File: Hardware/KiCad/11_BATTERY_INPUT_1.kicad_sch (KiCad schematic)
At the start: 0 parts

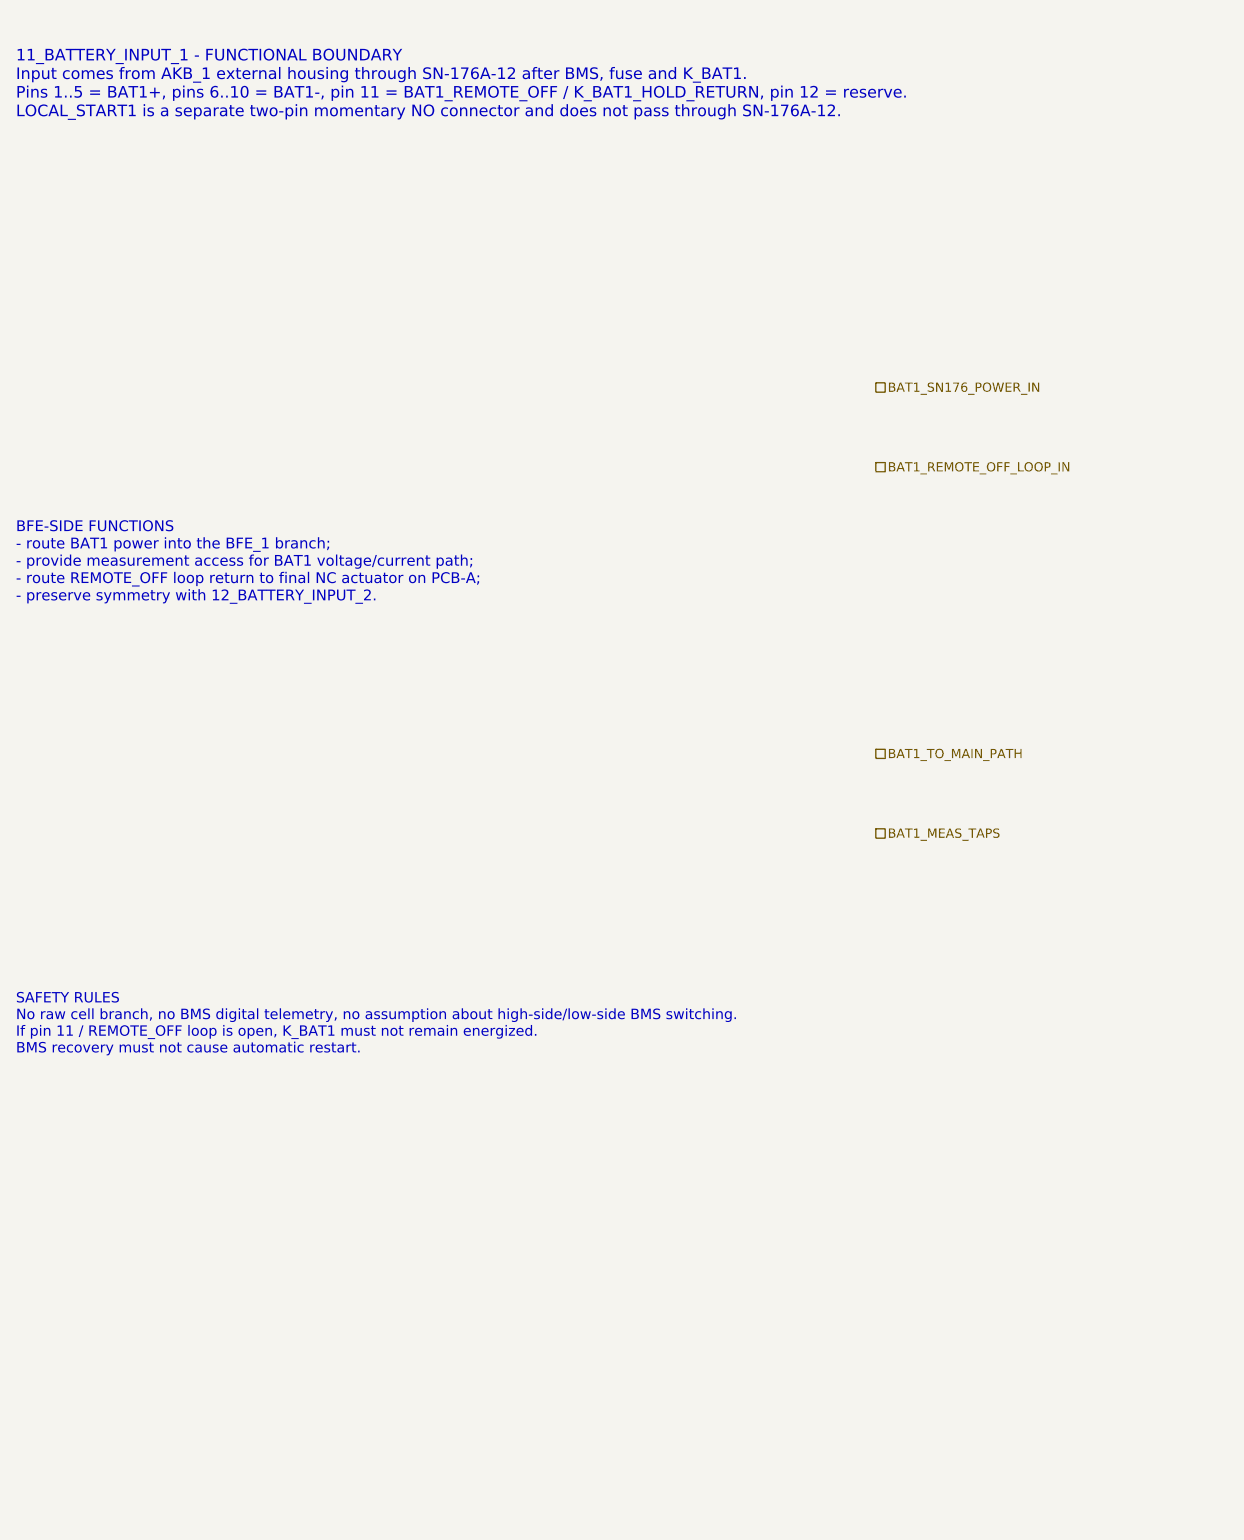
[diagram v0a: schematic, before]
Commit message: hardware: refine BAT1 input boundary level B
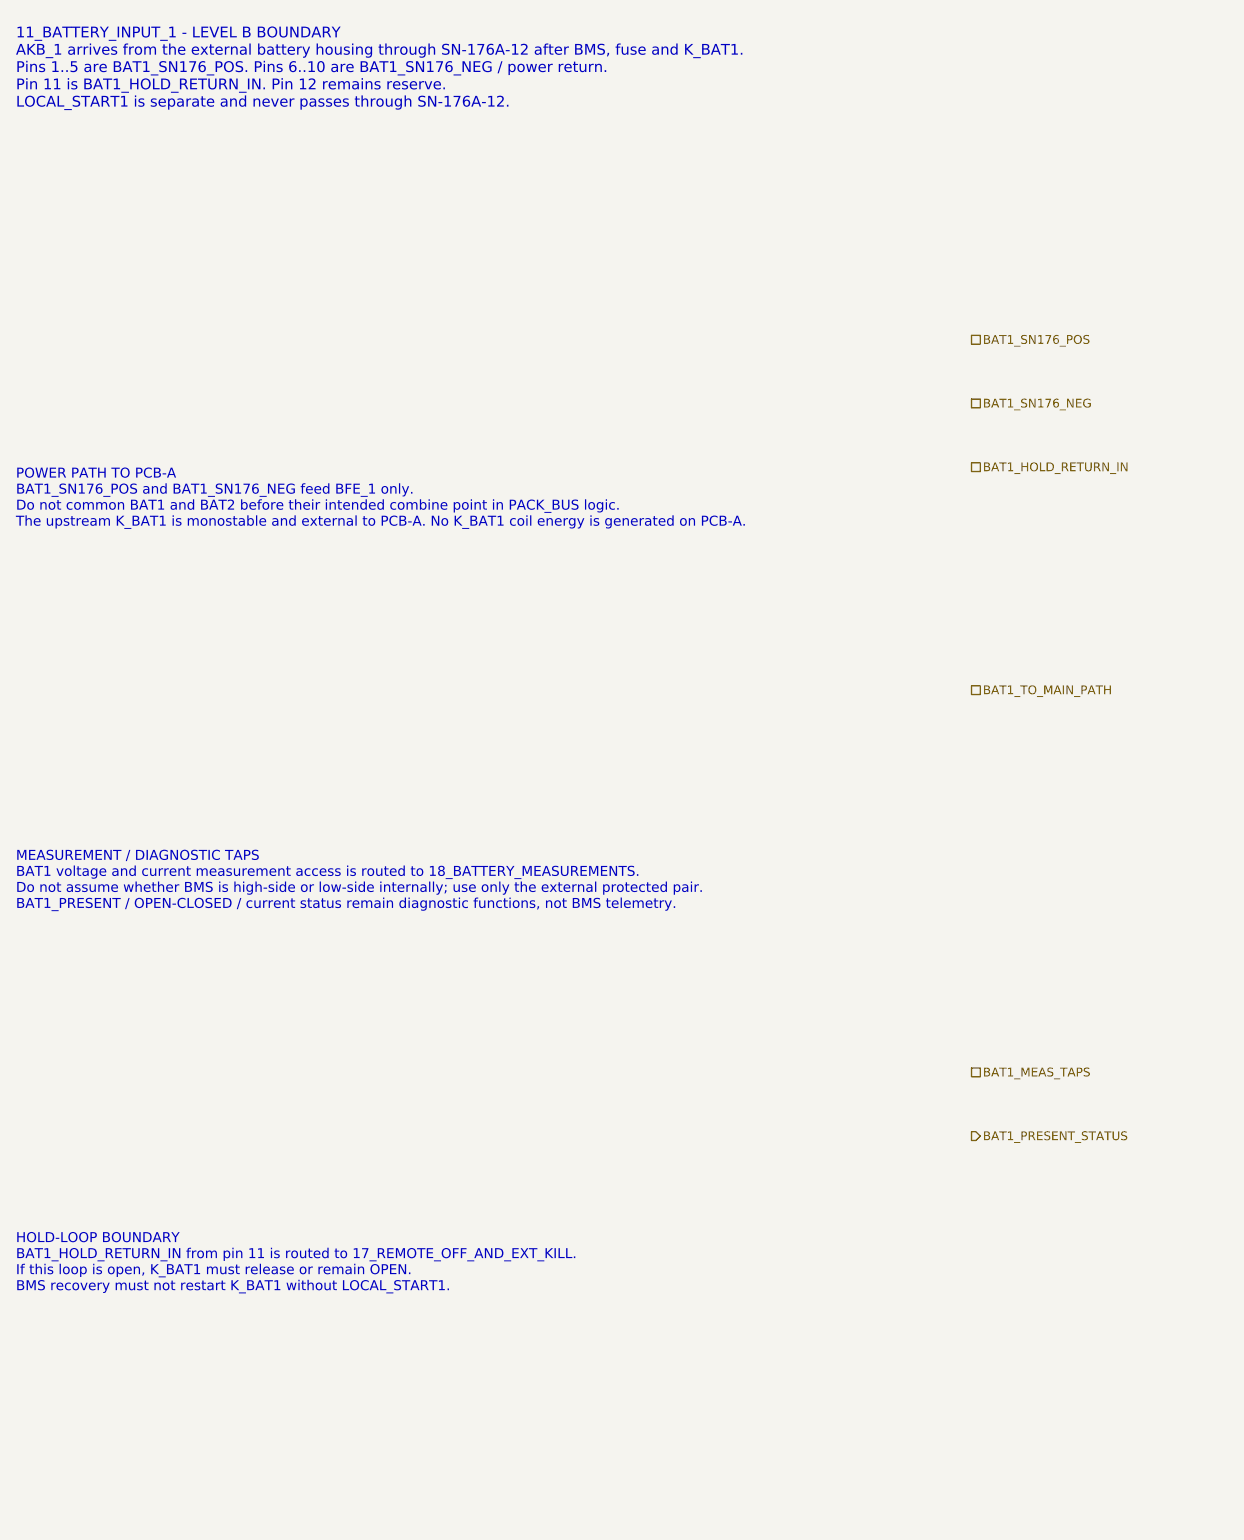
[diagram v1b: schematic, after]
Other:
- note added: "11_BATTERY_INPUT_1 - LEVEL B BOUNDARY AKB_1 arrives from the external battery housing through SN-176A-12 after BMS, fuse and K_BAT1. Pins 1..5 are BAT1_SN176_POS. Pins 6..10 are BAT1_SN176_NEG / power return. Pin 11 is BAT1_HOLD_RETURN_IN. Pin 12 remains reserve. LOCAL_START1 is separate and never passes through SN-176A-12."
- note added: "HOLD-LOOP BOUNDARY BAT1_HOLD_RETURN_IN from pin 11 is routed to 17_REMOTE_OFF_AND_EXT_KILL. If this loop is open, K_BAT1 must release or remain OPEN. BMS recovery must not restart K_BAT1 without LOCAL_START1."
- note added: "MEASUREMENT / DIAGNOSTIC TAPS BAT1 voltage and current measurement access is routed to 18_BATTERY_MEASUREMENTS. Do not assume whether BMS is high-side or low-side internally; use only the external protected pair. BAT1_PRESENT / OPEN-CLOSED / current status remain diagnostic functions, not BMS telemetry."
- note added: "POWER PATH TO PCB-A BAT1_SN176_POS and BAT1_SN176_NEG feed BFE_1 only. Do not common BAT1 and BAT2 before their intended combine point in PACK_BUS logic. The upstream K_BAT1 is monostable and external to PCB-A. No K_BAT1 coil energy is generated on PCB-A."
- note removed: "11_BATTERY_INPUT_1 - FUNCTIONAL BOUNDARY Input comes from AKB_1 external housing through SN-176A-12 after BMS, fuse and K_BAT1. Pins 1..5 = BAT1+, pins 6..10 = BAT1-, pin 11 = BAT1_REMOTE_OFF / K_BAT1_HOLD_RETURN, pin 12 = reserve. LOCAL_START1 is a separate two-pin momentary NO connector and does not pass through SN-176A-12."
- note removed: "BFE-SIDE FUNCTIONS - route BAT1 power into the BFE_1 branch; - provide measurement access for BAT1 voltage/current path; - route REMOTE_OFF loop return to final NC actuator on PCB-A; - preserve symmetry with 12_BATTERY_INPUT_2."
- note removed: "SAFETY RULES No raw cell branch, no BMS digital telemetry, no assumption about high-side/low-side BMS switching. If pin 11 / REMOTE_OFF loop is open, K_BAT1 must not remain energized. BMS recovery must not cause automatic restart."
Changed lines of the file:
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@@
 		(title "11_BATTERY_INPUT_1 - BFE input from AKB_1")
 		(date "2026-07-15")
-		(rev "A1")
+		(rev "B1")
 		(company "Gonoboben/plataVM")
-		(comment 1 "Architecture Level A: BFE-side input boundary for battery 1")
+		(comment 1 "Architecture Level B: BAT1 connector boundary and net naming")
 		(comment 2 "No connector family, fuse, current sensor or contactor model selected here")
 	)
-	(text "11_BATTERY_INPUT_1 - FUNCTIONAL BOUNDARY\nInput comes from AKB_1 external housing through SN-176A-12 after BMS, fuse and K_BAT1.\nPins 1..5 = BAT1+, pins 6..10 = BAT1-, pin 11 = BAT1_REMOTE_OFF / K_BAT1_HOLD_RETURN, pin 12 = reserve.\nLOCAL_START1 is a separate two-pin momentary NO connector and does not pass through SN-176A-12."
+	(text "11_BATTERY_INPUT_1 - LEVEL B BOUNDARY\nAKB_1 arrives from the external battery housing through SN-176A-12 after BMS, fuse and K_BAT1.\nPins 1..5 are BAT1_SN176_POS. Pins 6..10 are BAT1_SN176_NEG / power return.\nPin 11 is BAT1_HOLD_RETURN_IN. Pin 12 remains reserve.\nLOCAL_START1 is separate and never passes through SN-176A-12."
 		(exclude_from_sim no)
-		(at 12 18 0)
-		(effects (font (size 1.45 1.45)) (justify left))
+		(at 12 16 0)
+		(effects (font (size 1.35 1.35)) (justify left))
 		(uuid "bfe-dh-00000011-0000-4000-8000-000000000101")
 	)
-	(text "BFE-SIDE FUNCTIONS\n- route BAT1 power into the BFE_1 branch;\n- provide measurement access for BAT1 voltage/current path;\n- route REMOTE_OFF loop return to final NC actuator on PCB-A;\n- preserve symmetry with 12_BATTERY_INPUT_2."
+	(text "POWER PATH TO PCB-A\nBAT1_SN176_POS and BAT1_SN176_NEG feed BFE_1 only.\nDo not common BAT1 and BAT2 before their intended combine point in PACK_BUS logic.\nThe upstream K_BAT1 is monostable and external to PCB-A. No K_BAT1 coil energy is generated on PCB-A."
 		(exclude_from_sim no)
-		(at 12 78 0)
-		(effects (font (size 1.35 1.35)) (justify left))
+		(at 12 70 0)
+		(effects (font (size 1.25 1.25)) (justify left))
 		(uuid "bfe-dh-00000011-0000-4000-8000-000000000102")
 	)
-	(text "SAFETY RULES\nNo raw cell branch, no BMS digital telemetry, no assumption about high-side/low-side BMS switching.\nIf pin 11 / REMOTE_OFF loop is open, K_BAT1 must not remain energized.\nBMS recovery must not cause automatic restart."
+	(text "MEASUREMENT / DIAGNOSTIC TAPS\nBAT1 voltage and current measurement access is routed to 18_BATTERY_MEASUREMENTS.\nDo not assume whether BMS is high-side or low-side internally; use only the external protected pair.\nBAT1_PRESENT / OPEN-CLOSED / current status remain diagnostic functions, not BMS telemetry."
 		(exclude_from_sim no)
-		(at 12 136 0)
-		(effects (font (size 1.3 1.3)) (justify left))
+		(at 12 118 0)
+		(effects (font (size 1.25 1.25)) (justify left))
 		(uuid "bfe-dh-00000011-0000-4000-8000-000000000103")
 	)
-	(hierarchical_label "BAT1_SN176_POWER_IN" (shape passive) (exclude_from_sim no) (at 120 56 0) (effects (font (size 1.15 1.15)) (justify left)) (uuid "bfe-dh-00000011-0000-4000-8000-000000000201"))
-	(hierarchical_label "BAT1_REMOTE_OFF_LOOP_IN" (shape passive) (exclude_from_sim no) (at 120 66 0) (effects (font (size 1.15 1.15)) (justify left)) (uuid "bfe-dh-00000011-0000-4000-8000-000000000202"))
-	(hierarchical_label "BAT1_TO_MAIN_PATH" (shape passive) (exclude_from_sim no) (at 120 102 0) (effects (font (size 1.15 1.15)) (justify left)) (uuid "bfe-dh-00000011-0000-4000-8000-000000000203"))
-	(hierarchical_label "BAT1_MEAS_TAPS" (shape passive) (exclude_from_sim no) (at 120 112 0) (effects (font (size 1.15 1.15)) (justify left)) (uuid "bfe-dh-00000011-0000-4000-8000-000000000204"))
+	(text "HOLD-LOOP BOUNDARY\nBAT1_HOLD_RETURN_IN from pin 11 is routed to 17_REMOTE_OFF_AND_EXT_KILL.\nIf this loop is open, K_BAT1 must release or remain OPEN.\nBMS recovery must not restart K_BAT1 without LOCAL_START1."
+		(exclude_from_sim no)
+		(at 12 166 0)
+		(effects (font (size 1.25 1.25)) (justify left))
+		(uuid "bfe-dh-00000011-0000-4000-8000-000000000104")
+	)
+	(hierarchical_label "BAT1_SN176_POS" (shape passive) (exclude_from_sim no) (at 132 50 0) (effects (font (size 1.1 1.1)) (justify left)) (uuid "bfe-dh-00000011-0000-4000-8000-000000000201"))
+	(hierarchical_label "BAT1_SN176_NEG" (shape passive) (exclude_from_sim no) (at 132 58 0) (effects (font (size 1.1 1.1)) (justify left)) (uuid "bfe-dh-00000011-0000-4000-8000-000000000202"))
+	(hierarchical_label "BAT1_HOLD_RETURN_IN" (shape passive) (exclude_from_sim no) (at 132 66 0) (effects (font (size 1.1 1.1)) (justify left)) (uuid "bfe-dh-00000011-0000-4000-8000-000000000203"))
+	(hierarchical_label "BAT1_TO_MAIN_PATH" (shape passive) (exclude_from_sim no) (at 132 94 0) (effects (font (size 1.1 1.1)) (justify left)) (uuid "bfe-dh-00000011-0000-4000-8000-000000000204"))
+	(hierarchical_label "BAT1_MEAS_TAPS" (shape passive) (exclude_from_sim no) (at 132 142 0) (effects (font (size 1.1 1.1)) (justify left)) (uuid "bfe-dh-00000011-0000-4000-8000-000000000205"))
+	(hierarchical_label "BAT1_PRESENT_STATUS" (shape output) (exclude_from_sim no) (at 132 150 0) (effects (font (size 1.1 1.1)) (justify left)) (uuid "bfe-dh-00000011-0000-4000-8000-000000000206"))
 )
